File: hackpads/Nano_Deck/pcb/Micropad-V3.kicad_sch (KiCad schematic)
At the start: 51 parts, among them J1 OLED_128x64, SW1 RotaryEncoder_Switch, SW2 RotaryEncoder_Switch, U1 MCU_Seeed_XIAO_RP2040, U2 PCF8574A

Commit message: updated pcb
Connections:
- net RGB: now also U1.7 (PB08_A6_D6_TX); no longer U2.9 (P4)
- net Row -1: now also U2.4 (P0); no longer U1.7 (PB08_A6_D6_TX)
- net Row 0: now also U2.5 (P1); no longer U2.4 (P0)
- net Row 1: now also U2.6 (P2); no longer U2.5 (P1)
- net Row 2: now also U2.7 (P3); no longer U2.6 (P2)
- net Row 3: now also U2.9 (P4); no longer U2.7 (P3)
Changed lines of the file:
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@@
+	)
+	(junction
+		(at 38.1 85.09)
+		(diameter 0)
+		(color 0 0 0 0)
 	)
 	(junction
@@
 	(wire
 		(pts
+			(xy 55.88 105.41) (xy 59.69 105.41)
+		)
+		(stroke
+			(width 0)
+			(type default)
+		)
+	)
+	(wire
+		(pts
 			(xy 171.45 146.05) (xy 171.45 147.32)
 		)
@@
 	(wire
 		(pts
+			(xy 55.88 110.49) (xy 59.69 110.49)
+		)
+		(stroke
+			(width 0)
+			(type default)
+		)
+	)
+	(wire
+		(pts
 			(xy 196.85 138.43) (xy 199.39 138.43)
 		)
@@
 	(wire
 		(pts
+			(xy 55.88 107.95) (xy 59.69 107.95)
+		)
+		(stroke
+			(width 0)
+			(type default)
+		)
+	)
+	(wire
+		(pts
 			(xy 207.01 146.05) (xy 207.01 147.32)
 		)
@@
 	(wire
 		(pts
+			(xy 38.1 85.09) (xy 40.64 85.09)
+		)
+		(stroke
+			(width 0)
+			(type default)
+		)
+	)
+	(wire
+		(pts
 			(xy 118.11 130.81) (xy 118.11 132.08)
 		)
@@
 	(wire
 		(pts
+			(xy 55.88 113.03) (xy 59.69 113.03)
+		)
+		(stroke
+			(width 0)
+			(type default)
+		)
+	)
+	(wire
+		(pts
 			(xy 171.45 130.81) (xy 171.45 132.08)
 		)
@@
 	(wire
 		(pts
+			(xy 55.88 102.87) (xy 58.42 102.87)
+		)
+		(stroke
+			(width 0)
+			(type default)
+		)
+	)
+	(wire
+		(pts
 			(xy 72.39 138.43) (xy 74.93 138.43)
 		)
@@
 	(wire
 		(pts
+			(xy 31.75 85.09) (xy 38.1 85.09)
+		)
+		(stroke
+			(width 0)
+			(type default)
+		)
+	)
+	(wire
+		(pts
 			(xy 100.33 130.81) (xy 100.33 132.08)
 		)
@@
 	(global_label "Row 0"
 		(shape input)
-		(at 55.88 102.87 0)
-		(fields_autoplaced yes)
-		(effects
-			(font
-				(size 1.27 1.27)
-			)
-			(justify left)
-		)
-		(property "Intersheetrefs" "${INTERSHEET_REFS}"
-			(at 64.7918 102.87 0)
+		(at 59.69 105.41 0)
+		(fields_autoplaced yes)
+		(effects
+			(font
+				(size 1.27 1.27)
+			)
+			(justify left)
+		)
+		(property "Intersheetrefs" "${INTERSHEET_REFS}"
+			(at 68.6018 105.41 0)
 			(effects
 				(font
@@
 	(global_label "RGB"
 		(shape input)
-		(at 55.88 113.03 0)
-		(fields_autoplaced yes)
-		(effects
-			(font
-				(size 1.27 1.27)
-			)
-			(justify left)
-		)
-		(property "Intersheetrefs" "${INTERSHEET_REFS}"
-			(at 62.6752 113.03 0)
-			(effects
-				(font
-					(size 1.27 1.27)
-				)
-				(justify left)
+		(at 31.75 85.09 180)
+		(fields_autoplaced yes)
+		(effects
+			(font
+				(size 1.27 1.27)
+			)
+			(justify right)
+		)
+		(property "Intersheetrefs" "${INTERSHEET_REFS}"
+			(at 24.9548 85.09 0)
+			(effects
+				(font
+					(size 1.27 1.27)
+				)
+				(justify right)
 				(hide yes)
 			)
@@
 	(global_label "Row 3"
 		(shape input)
-		(at 55.88 110.49 0)
-		(fields_autoplaced yes)
-		(effects
-			(font
-				(size 1.27 1.27)
-			)
-			(justify left)
-		)
-		(property "Intersheetrefs" "${INTERSHEET_REFS}"
-			(at 64.7918 110.49 0)
+		(at 59.69 113.03 0)
+		(fields_autoplaced yes)
+		(effects
+			(font
+				(size 1.27 1.27)
+			)
+			(justify left)
+		)
+		(property "Intersheetrefs" "${INTERSHEET_REFS}"
+			(at 68.6018 113.03 0)
 			(effects
 				(font
@@
 	(global_label "Row 1"
 		(shape input)
-		(at 55.88 105.41 0)
-		(fields_autoplaced yes)
-		(effects
-			(font
-				(size 1.27 1.27)
-			)
-			(justify left)
-		)
-		(property "Intersheetrefs" "${INTERSHEET_REFS}"
-			(at 64.7918 105.41 0)
+		(at 59.69 107.95 0)
+		(fields_autoplaced yes)
+		(effects
+			(font
+				(size 1.27 1.27)
+			)
+			(justify left)
+		)
+		(property "Intersheetrefs" "${INTERSHEET_REFS}"
+			(at 68.6018 107.95 0)
 			(effects
 				(font
@@
 	(global_label "Row -1"
 		(shape input)
-		(at 38.1 85.09 180)
+		(at 58.42 102.87 0)
+		(fields_autoplaced yes)
+		(effects
+			(font
+				(size 1.27 1.27)
+			)
+			(justify left)
+		)
+		(property "Intersheetrefs" "${INTERSHEET_REFS}"
+			(at 68.9042 102.87 0)
+			(effects
+				(font
+					(size 1.27 1.27)
+				)
+				(justify left)
+				(hide yes)
+			)
+		)
+	)
+	(global_label "Column 3"
+		(shape input)
+		(at 38.1 77.47 180)
 		(fields_autoplaced yes)
 		(effects
@@
 		)
 		(property "Intersheetrefs" "${INTERSHEET_REFS}"
-			(at 27.6158 85.09 0)
+			(at 25.8622 77.47 0)
 			(effects
 				(font
@@
 		)
 	)
-	(global_label "Column 3"
-		(shape input)
-		(at 38.1 77.47 180)
-		(fields_autoplaced yes)
-		(effects
-			(font
-				(size 1.27 1.27)
-			)
-			(justify right)
-		)
-		(property "Intersheetrefs" "${INTERSHEET_REFS}"
-			(at 25.8622 77.47 0)
-			(effects
-				(font
-					(size 1.27 1.27)
-				)
-				(justify right)
-				(hide yes)
-			)
-		)
-	)
 	(global_label "Row 2"
 		(shape input)
@@
 	(global_label "Row 2"
 		(shape input)
-		(at 55.88 107.95 0)
-		(fields_autoplaced yes)
-		(effects
-			(font
-				(size 1.27 1.27)
-			)
-			(justify left)
-		)
-		(property "Intersheetrefs" "${INTERSHEET_REFS}"
-			(at 64.7918 107.95 0)
-			(effects
-				(font
+		(at 59.69 110.49 0)
+		(fields_autoplaced yes)
+		(effects
+			(font
+				(size 1.27 1.27)
+			)
+			(justify left)
+		)
+		(property "Intersheetrefs" "${INTERSHEET_REFS}"
+			(at 68.6018 110.49 0)
+			(effects
+				(font

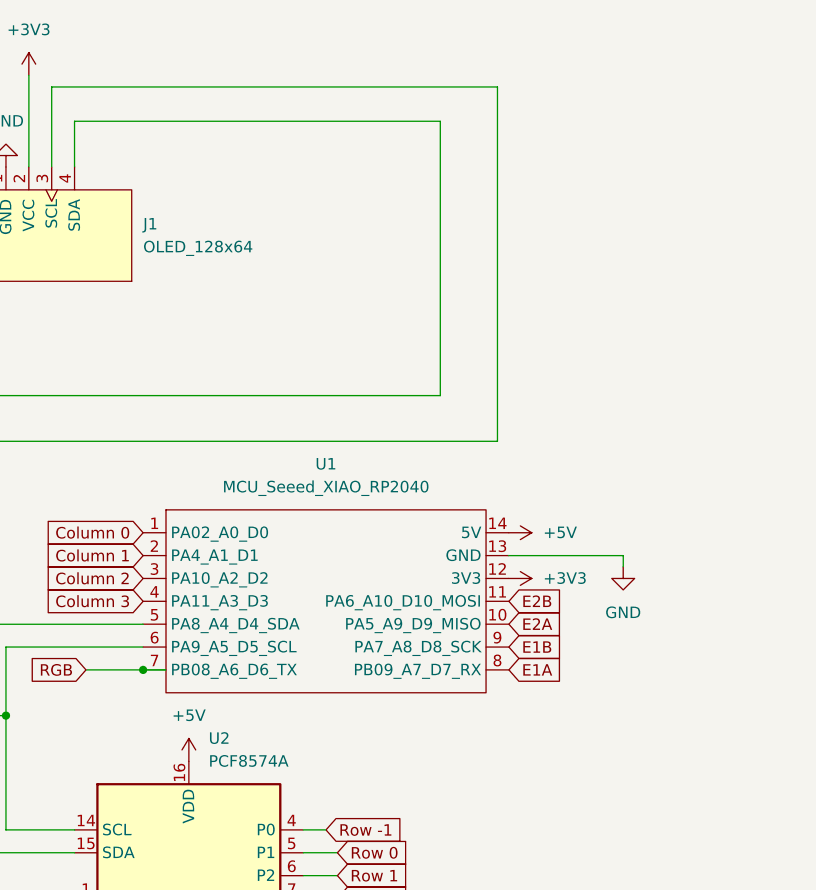
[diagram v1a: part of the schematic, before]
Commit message: added resistors for 12c
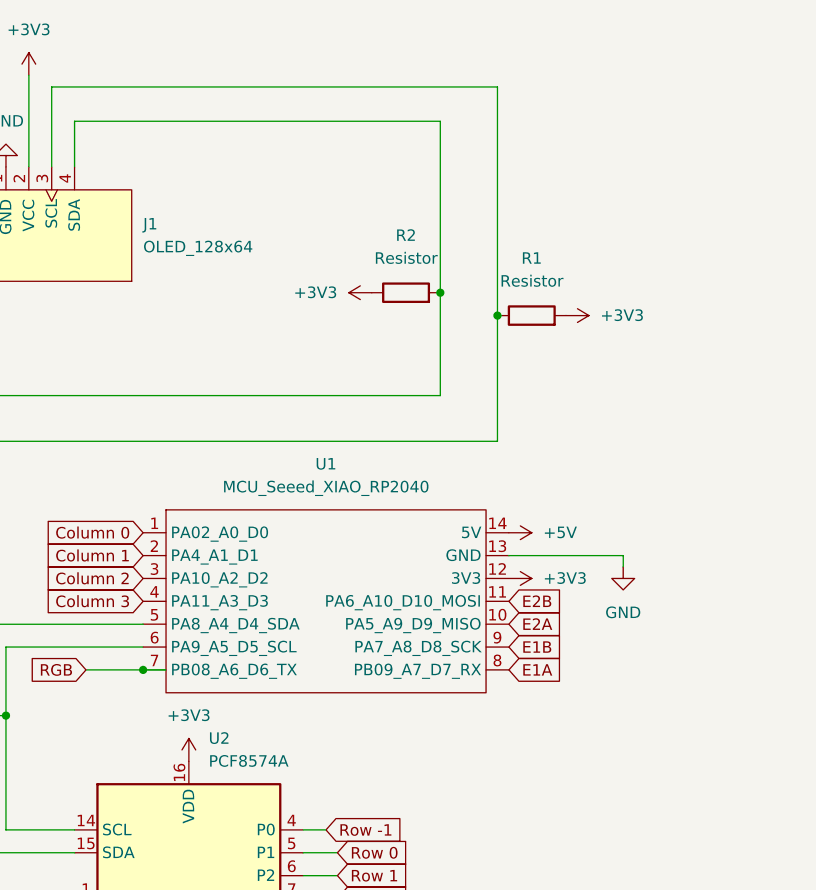
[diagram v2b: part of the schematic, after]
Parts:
- added R1, R2: Resistor, Resistor_THT:R_Axial_DIN0204_L3.6mm_D1.6mm_P5.08mm_Horizontal, symbol ScottoKeebs:Placeholder_Resistor
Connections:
- net +3V3: now also U2.16 (VDD), R1.2, R2.1
- net +5V: no longer U2.16 (VDD)
- net at J1.4 (SDA), U1.5 (PA8_A4_D4_SDA), U2.15 (SDA): now also R2.2
- net at J1.3 (SCL), U1.6 (PA9_A5_D5_SCL), U2.14 (SCL): now also R1.1
